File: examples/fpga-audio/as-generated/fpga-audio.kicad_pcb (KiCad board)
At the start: 2 copper layers, 100 x 84 mm, 40 parts, among them J1 3V3 IN, J2 AUDIO OUT, J3 SPI PROG, U1 iCE40UP5K, U2 PCM5102A, U3 AP2112K-1.2, U4 W25Q32JV, X1 12MHz

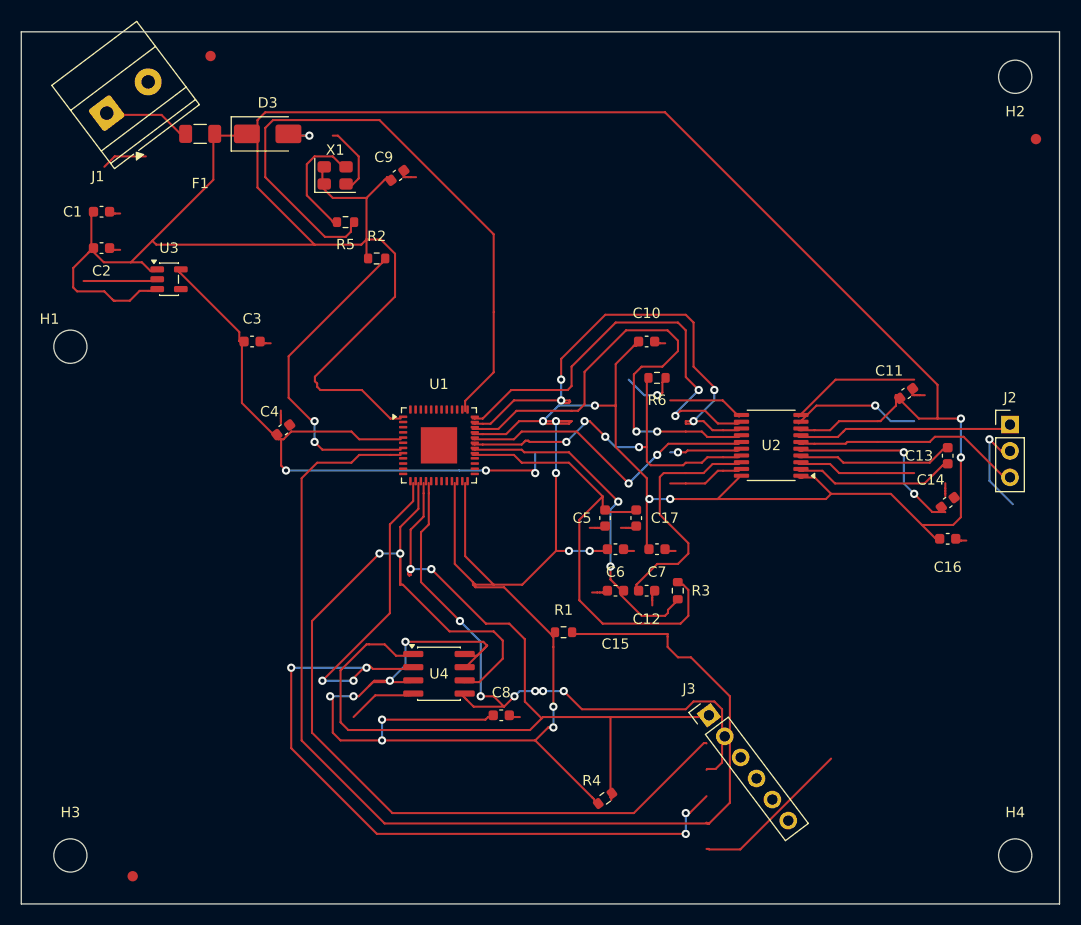
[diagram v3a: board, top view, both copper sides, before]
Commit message: feat(examples): route the nets with something to lose first, and never behind a plain one
The reviewer circled a column of ten vias on the motor driver: the four
0.4 mm bridge outputs and nFAULT each hopped under one 0.3 mm logic input
that had toured the west end of the board and been promoted to the front
for it. Two causes: the search charged the plane surcharge on a link the
design had declared on the back, and the header pin sat on the far side of
AIN2's stated lane from its via.

The routing order now has two classes. A link wider than the board's
thinnest, or on a net the design names in priority_nets, is routed while
the board is empty; a rip-up or a detour chase promotes a plain link only
to the front of the plain links, so it goes round. A plain link with no
lane even there is lifted ahead of the priority nets and the log says so:
a floorplan with no room, the placement's problem. A link declared on the
back and kept there pays the router's ordinary rate. resolve_routes and
the two helpers join the route-cache key, as does priority_nets.

Per board: motor-driver's J4 pins reordered to the order the drops land,
and AIN2's lane turns where its last leg is a 45; the bridge outputs and
nFAULT now route straight with zero vias, on the first pass. opamp-filter
names its filter path and fences its three connectors; fpga-audio names
its rails (distributed at signal width by design), the clock and the I2S
bus. All five cold-route clean: gates, contracts and KiCad DRC pass.

Also fix the loop cutter: it split a back-side run at a front-side pad it
passed under, manufactured a node the front stub shared, read a cycle and
cut the stub and its via. The split now respects the pad's layer, with a
test that shows the old cutter losing the via.

Co-Authored-By: Claude Fable 5.1 <noreply@anthropic.com>
Claude-Session: https://claude.ai/code/session_01XQE7UkE9WTSMW3oZ3kLeCt
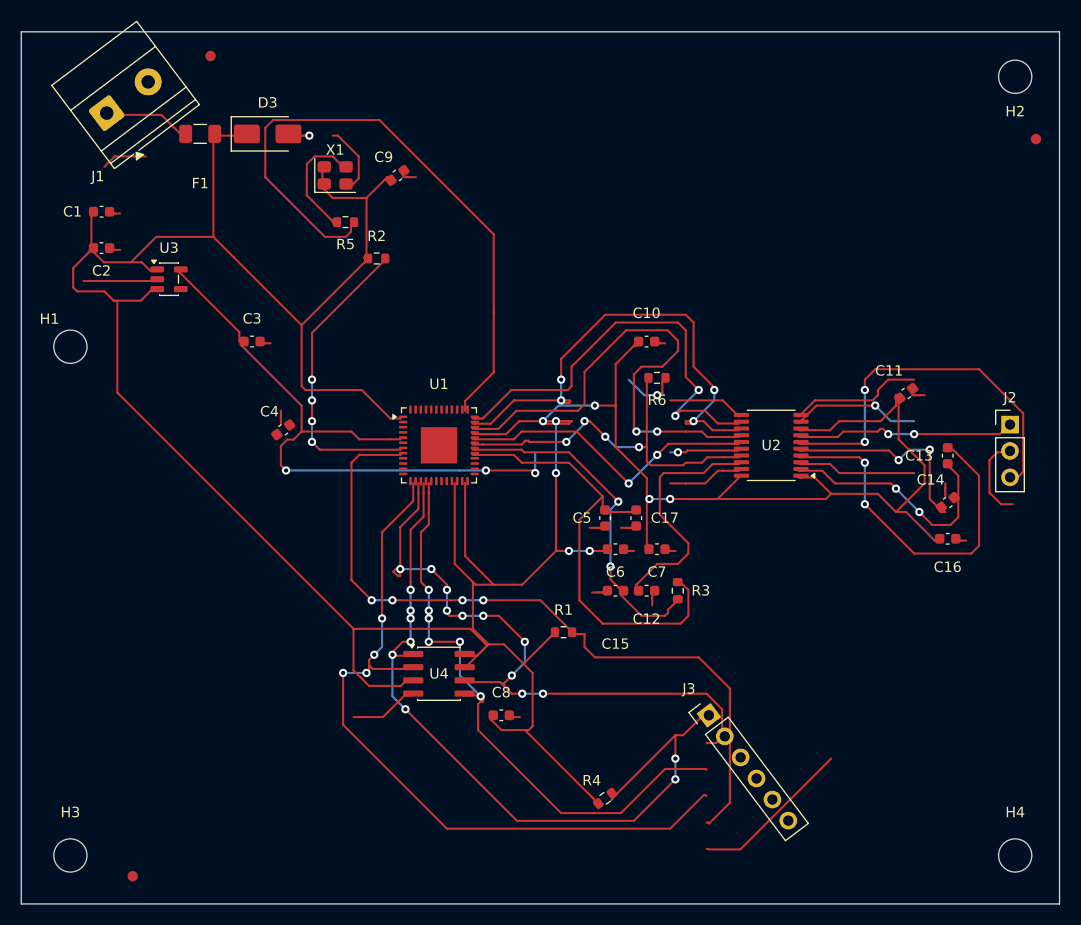
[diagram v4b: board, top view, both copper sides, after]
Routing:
- net +3V3: track 460.3 -> 362.3 mm, vias 18 -> 8
- net /CRESET: track 110.3 -> 72.2 mm, vias 0 -> 4
- net /SPI_SCK: track 98.2 -> 63.4 mm, vias 2 -> 10
- net /SPI_SO: track 93.6 -> 72.3 mm, vias 6 -> 4
- net /CAPM: track 14.9 -> 34.9 mm, vias 0 -> 2
- net /OUTL: track 22.1 -> 37.3 mm, vias 0 -> 2
- net /SPI_SS: track 89.9 -> 74.8 mm, vias 2 -> 8
- net /CAPP: track 15.4 -> 23.5 mm, vias 0 -> 2
- net /SPI_SI: track 60.3 -> 58.1 mm
- net /CDONE: track 31.1 -> 29.2 mm, vias 2 -> 4
- net /VNEG: track 18.4 -> 20.2 mm
- net GND: track 136.0 -> 134.7 mm, vias 5 -> 4
- net /OUTR: track 20.6 -> 21.0 mm, vias 0 -> 2

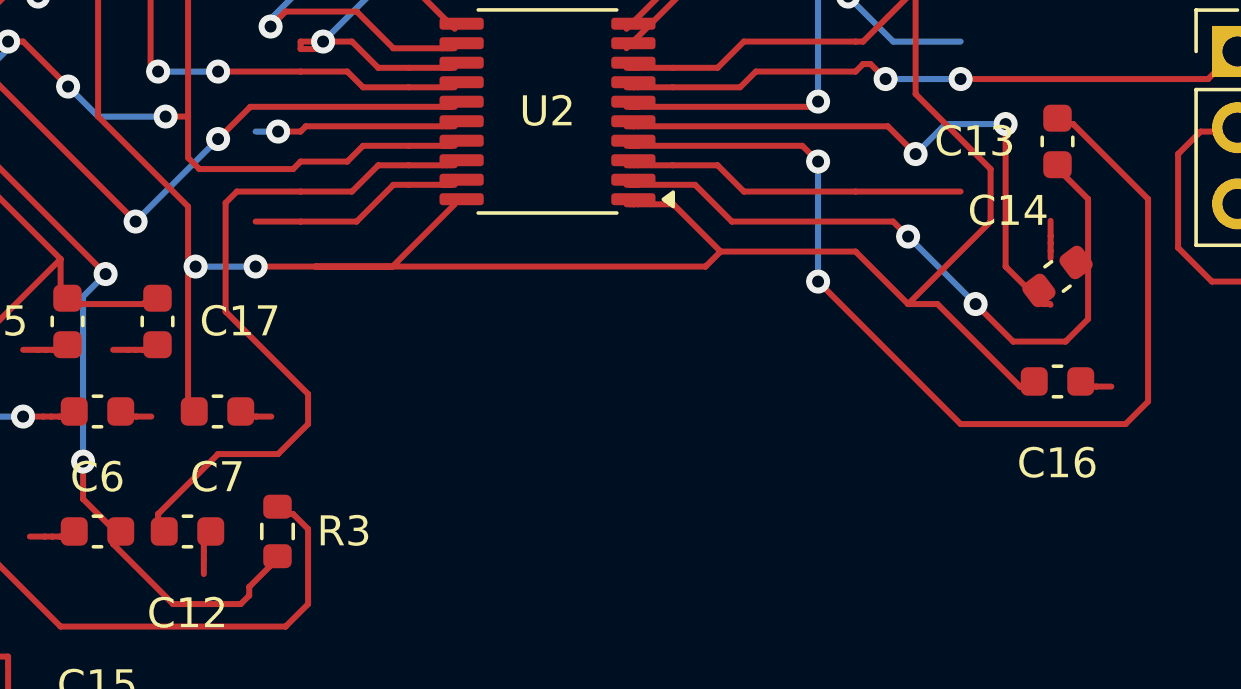
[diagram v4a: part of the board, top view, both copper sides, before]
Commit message: feat(examples,pcb-review): line up connector legends, and keep silk from under other parts
Two things the reviewer asked of the silk. A connector's pin names should
line up so their positions can be read at a glance, and nothing should be
printed where a fitted part will hide it.

Legends are laid out a row at a time: every pin of a connector gets the
same side and distance from the pad row, anchored on its own pin, and
turned a quarter to stand up from the pins where the names are wider than
the pitch. Only a row that cannot be lined up clean falls back to placing
each pin on its own, with a slide bounded so the pin it names stays the
nearest one.

Other parts' courtyards now weigh as much as pads for every string the
generator places - designators, legends, the board id - since a body
hides ink the moment it is fitted. The motor driver's fuse had its name a
millimetre inside the bulk capacitor's outline; the op-amp board's name
ran across a test point standing in the name's strip, and the test point
moves out of it. silk.under_part reports a string inside a foreign
courtyard on its own side, and the board parser now carries a string's
justification so the review measures a legend where it prints rather
than half a string away.

Co-Authored-By: Claude Fable 5.1 <noreply@anthropic.com>
Claude-Session: https://claude.ai/code/session_01XQE7UkE9WTSMW3oZ3kLeCt
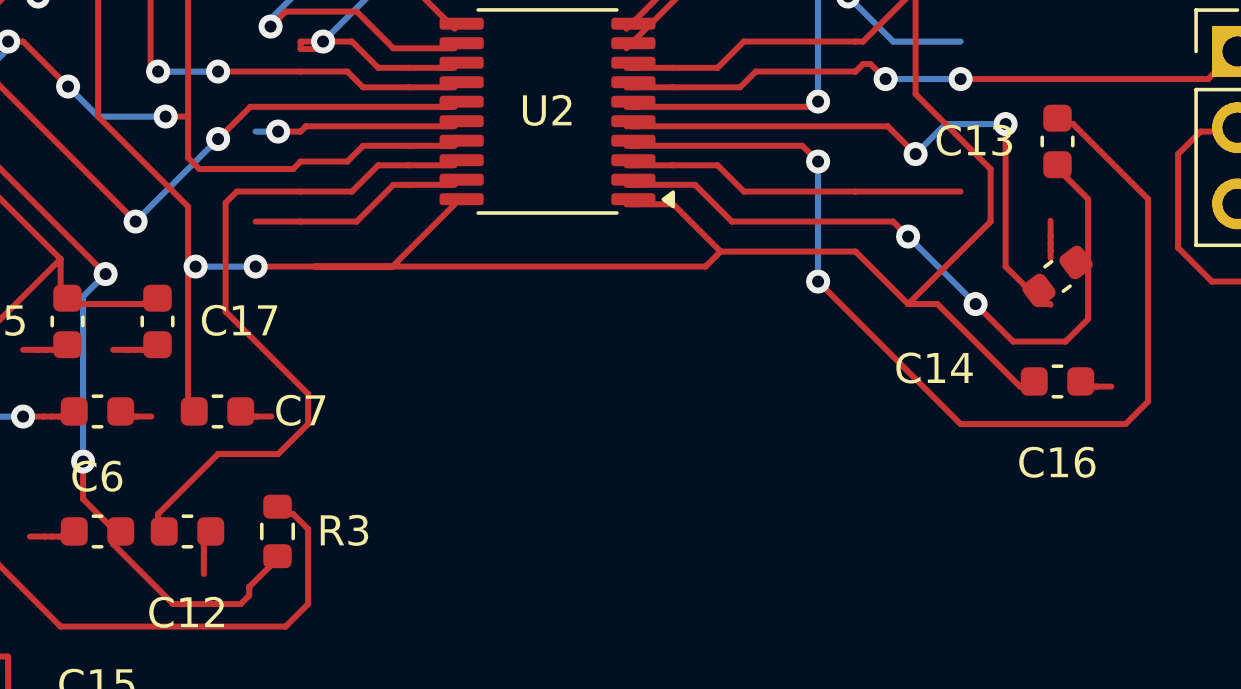
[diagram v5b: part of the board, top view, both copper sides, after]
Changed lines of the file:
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@@
     (tags "capacitor")
     (property "Reference" "C14"
-      (at 0 -2.73 0)
+      (at -5.13 0 0)
       (layer "F.SilkS")
       (effects
@@
     )
     (property "Datasheet" "https://product.samsungsem.com/mlcc/CL10A225KO8NNNC.do"
-      (at 0 -2.73 0)
+      (at -5.13 0 0)
       (layer "F.Fab")
       (hide yes)
@@
     (tags "capacitor")
     (property "Reference" "C7"
-      (at 0 2.195 0)
+      (at 2.795 0 0)
       (layer "F.SilkS")
       (effects
@@
     )
     (property "Datasheet" "https://product.samsungsem.com/mlcc/CL10B104KB8NNNC.do"
-      (at 0 2.195 0)
-      (layer "F.Fab")
-      (hide yes)
+      (at 2.795 0 0)
+      (layer "F.Fab")
+      (hide yes)
